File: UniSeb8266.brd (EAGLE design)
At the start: 72 x 100 mm, 31 parts, among them IC1 WEMOS-D1-MINI, IC2 GY-BME280-3.3, IC3 LM3940, IC4 MCP23008SS, IC5 RT9400, IC6 AMS5915, J1 22-27-2031-03, X61 JST-XH-05-PIN-LONG-PAD, X7 0446200002

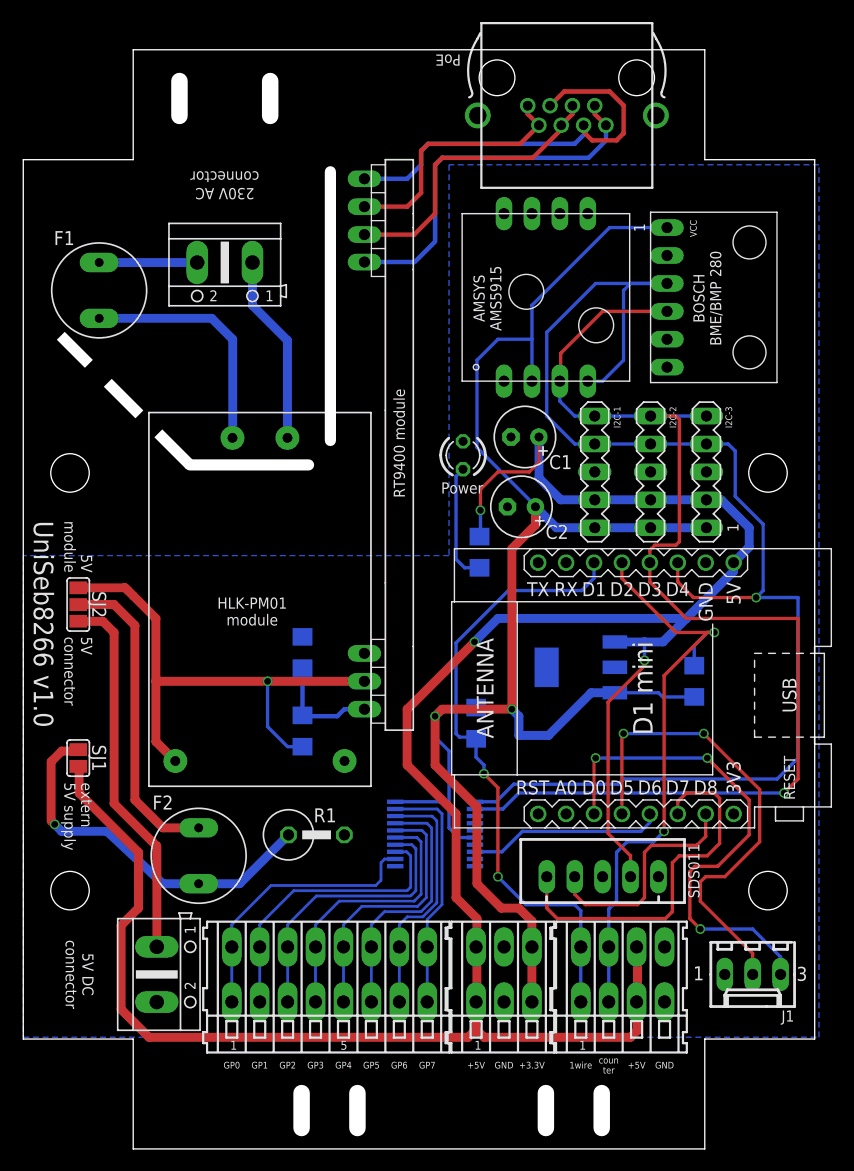
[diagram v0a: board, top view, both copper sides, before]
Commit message: Changed the fixed voltage regulator to AMS1117/LM1117 and the output capacitor.
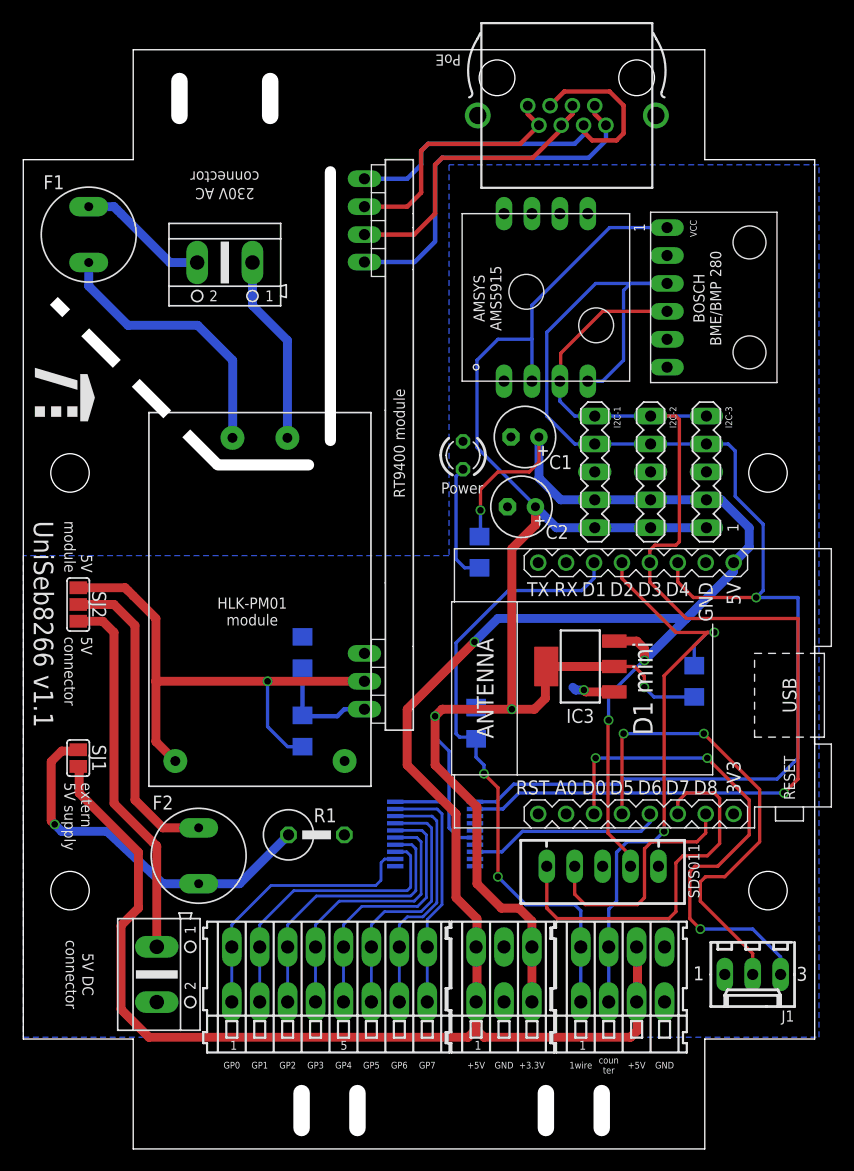
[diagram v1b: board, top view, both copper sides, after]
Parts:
- C2: value 100µF -> 22µF
- IC3: value LM3940 -> AMS1117-3.3; device linear:SOT223 -> lm1117:SOT223
- moved F1 5.17 mm to (5.95, 83.2)
- moved X61 0.95 mm to (52.7, 25.7), turned to 180 degrees
- moved IC3 0.09 mm to (50.7, 43.9), flipped to the top, turned to 90 degrees
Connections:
- net +3V3: now also IC3.2, IC3.TAB; no longer IC3.3
- net +5V: now also IC3.3, X61.2; no longer IC3.1, X61.4
- net GND: now also IC3.1; no longer IC3.2, IC3.4
- net SDS_RX: now also X61.4; no longer X61.2
- net SDS_TX: now also X61.5; no longer X61.1
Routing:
- net GND: track 0.00 -> 3.95 mm, vias 0 -> 1
- net N$2: track 21.9 -> 25.1 mm
- net N$1: track 8.92 -> 12.0 mm
- net +3V3: track 159.0 -> 160.2 mm, vias 2 -> 3
- net SDS_RX: track 20.9 -> 21.9 mm
- net SDS_TX: track 34.0 -> 34.9 mm
- net +5V: track 221.6 -> 221.1 mm, vias 3 -> 4
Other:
- outline, holes or cut-outs redrawn
- board text added: "UniSeb8266 v1.1"
- board text removed: "UniSeb8266 v1.0"

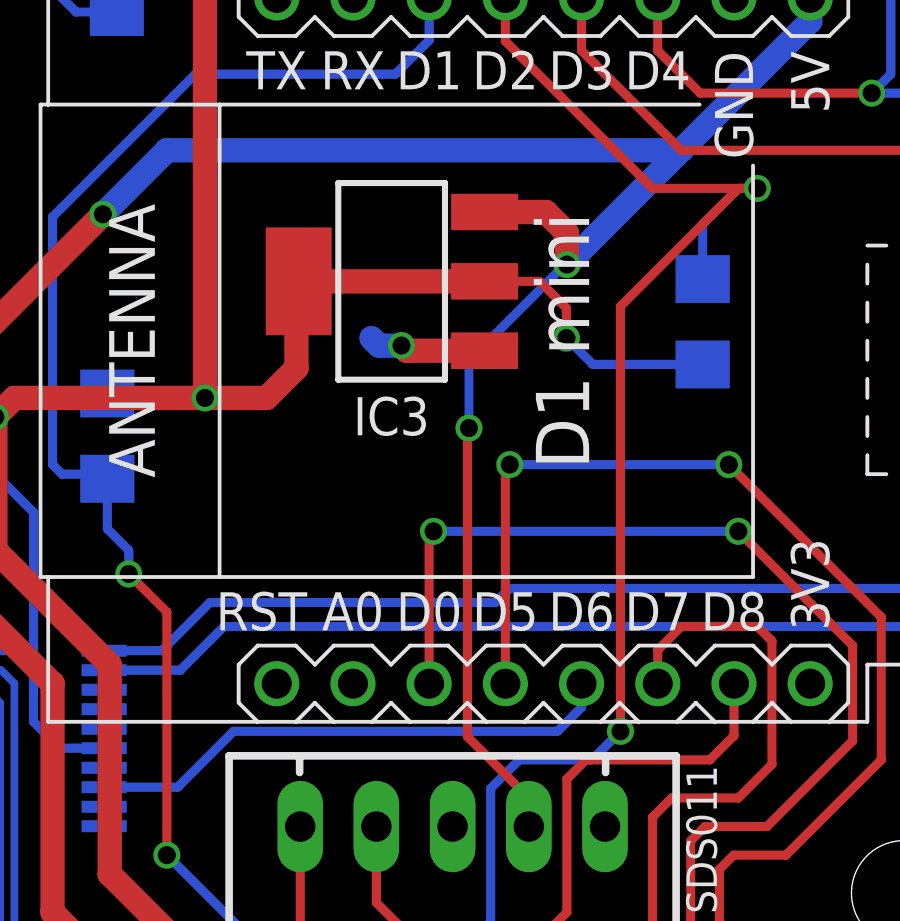
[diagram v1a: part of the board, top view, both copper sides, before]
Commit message: Changed placement of IC3 to bottom layer.
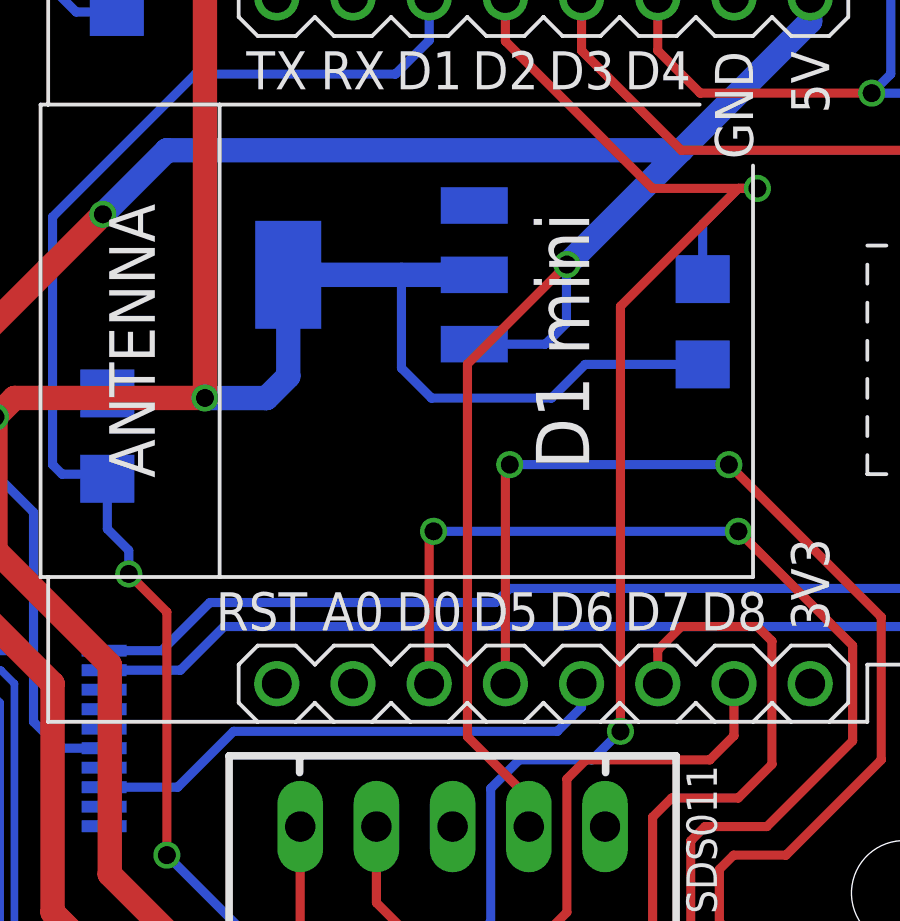
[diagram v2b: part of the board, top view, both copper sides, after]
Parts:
- moved IC3 0.41 mm to (50.3, 44.1), flipped to the bottom, turned to 270 degrees
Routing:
- net +3V3: track 160.2 -> 165.3 mm, vias 3 -> 2
- net GND: track 3.95 -> 0.00 mm, vias 1 -> 0
- net +5V: track 221.1 -> 222.3 mm, vias 4 -> 3
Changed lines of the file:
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@@
 </element>
 <element name="U$2" library="HLK" package="HLK-PM01" value="HLK-PM01" x="11.43" y="66.9925" rot="R270"/>
-<element name="IC3" library="lm1117" package="SOT223" value="AMS1117-3.3" x="50.673" y="43.8912" rot="R90"/>
+<element name="IC3" library="lm1117" package="SOT223" value="AMS1117-3.3" x="50.327" y="44.1088" rot="MR270"/>
 </elements>
 <signals>
@@
 <contactref element="X2" pad="2"/>
 <contactref element="IC3" pad="1"/>
-<wire x1="53.772" y1="41.5802" x2="51.1698" y2="41.5802" width="0.8128" layer="1"/>
-<wire x1="51.1698" y1="41.5802" x2="51" y2="41.75" width="0.8128" layer="1"/>
-<via x="51" y="41.75" extent="1-16" drill="0.6"/>
-<wire x1="51" y1="41.75" x2="50.25" y2="41.75" width="0.8128" layer="16"/>
-<wire x1="50.25" y1="41.75" x2="50" y2="42" width="0.8128" layer="16"/>
 </signal>
 <signal name="+5V">
@@
 <wire x1="55.245" y1="26.67" x2="55.245" y2="25.7175" width="0.3048" layer="1"/>
 <contactref element="IC3" pad="3"/>
-<wire x1="53.772" y1="46.2022" x2="55.8128" y2="46.2022" width="0.8128" layer="1"/>
-<wire x1="55.8128" y1="46.2022" x2="56.515" y2="45.5" width="0.8128" layer="1"/>
-<wire x1="56.515" y1="45.5" x2="56.515" y2="44.45" width="0.8128" layer="1"/>
 <wire x1="56.515" y1="44.45" x2="56.45" y2="44.45" width="0.3048" layer="16"/>
-<wire x1="56.45" y1="44.45" x2="54" y2="42" width="0.3048" layer="16"/>
-<wire x1="54" y1="42" x2="53.5" y2="41.5" width="0.3048" layer="16"/>
-<wire x1="53.2" y1="28.715" x2="53.2" y2="38.95" width="0.3048" layer="1"/>
-<wire x1="53.2" y1="38.95" x2="53.25" y2="39" width="0.3048" layer="1"/>
-<via x="53.25" y="39" extent="1-16" drill="0.6"/>
-<wire x1="53.25" y1="39" x2="53.25" y2="41.25" width="0.3048" layer="16"/>
-<wire x1="53.25" y1="41.25" x2="53.5" y2="41.5" width="0.3048" layer="16"/>
+<wire x1="53.2" y1="28.715" x2="53.2" y2="41.135" width="0.3048" layer="1"/>
+<wire x1="53.2" y1="41.135" x2="56.515" y2="44.45" width="0.3048" layer="1"/>
+<wire x1="53.426" y1="41.7978" x2="55.7978" y2="41.7978" width="0.3048" layer="16"/>
+<wire x1="55.7978" y1="41.7978" x2="56.5" y2="42.5" width="0.3048" layer="16"/>
+<wire x1="56.5" y1="42.5" x2="56.5" y2="44.435" width="0.3048" layer="16"/>
+<wire x1="56.5" y1="44.435" x2="56.515" y2="44.45" width="0.3048" layer="16"/>
 </signal>
 <signal name="SDS_TX">
@@
 <contactref element="IC3" pad="2"/>
 <contactref element="IC3" pad="TAB"/>
-<wire x1="44.45" y1="40.005" x2="46.505" y2="40.005" width="0.8128" layer="1"/>
-<wire x1="46.505" y1="40.005" x2="47.5" y2="41" width="0.8128" layer="1"/>
-<wire x1="47.5" y1="41" x2="47.5" y2="43.8172" width="0.8128" layer="1"/>
-<wire x1="47.5" y1="43.8172" x2="47.574" y2="43.8912" width="0.8128" layer="1"/>
-<wire x1="53.772" y1="43.8912" x2="47.574" y2="43.8912" width="0.8128" layer="1"/>
-<wire x1="53.772" y1="43.8912" x2="55.6088" y2="43.8912" width="0.3048" layer="1"/>
-<wire x1="55.6088" y1="43.8912" x2="56.5" y2="43" width="0.3048" layer="1"/>
-<wire x1="56.5" y1="43" x2="56.5" y2="42" width="0.3048" layer="1"/>
-<via x="56.5" y="42" extent="1-16" drill="0.6"/>
-<wire x1="56.5" y1="42" x2="57.377" y2="41.123" width="0.3048" layer="16"/>
-<wire x1="61.04" y1="41.123" x2="57.377" y2="41.123" width="0.3048" layer="16"/>
+<wire x1="61.04" y1="41.123" x2="57.123" y2="41.123" width="0.3048" layer="16"/>
+<wire x1="47.228" y1="44.1088" x2="47.228" y2="40.728" width="0.8128" layer="16"/>
+<wire x1="47.228" y1="40.728" x2="46.5" y2="40" width="0.8128" layer="16"/>
+<wire x1="46.5" y1="40" x2="44.455" y2="40" width="0.8128" layer="16"/>
+<wire x1="44.455" y1="40" x2="44.45" y2="40.005" width="0.8128" layer="16"/>
+<wire x1="47.228" y1="44.1088" x2="51" y2="44.1088" width="0.8128" layer="16"/>
+<wire x1="51" y1="44.1088" x2="53.426" y2="44.1088" width="0.8128" layer="16"/>
+<wire x1="57.123" y1="41.123" x2="56" y2="40" width="0.3048" layer="16"/>
+<wire x1="56" y1="40" x2="52" y2="40" width="0.3048" layer="16"/>
+<wire x1="52" y1="40" x2="51" y2="41" width="0.3048" layer="16"/>
+<wire x1="51" y1="41" x2="51" y2="44.1088" width="0.3048" layer="16"/>
 </signal>
 <signal name="COUNTER">
